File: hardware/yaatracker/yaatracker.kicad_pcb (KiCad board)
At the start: 2 copper layers, 63 parts, among them J1 USB_MINI, P1 TP_URX, P10 BATT, P11 MBUTTON2, P12 ICSP_CONN5, P13 I2C_SCREEN, P14 R_VCC, P15 GPS_DE9, P16 RADIO_DE9, P17 SW5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

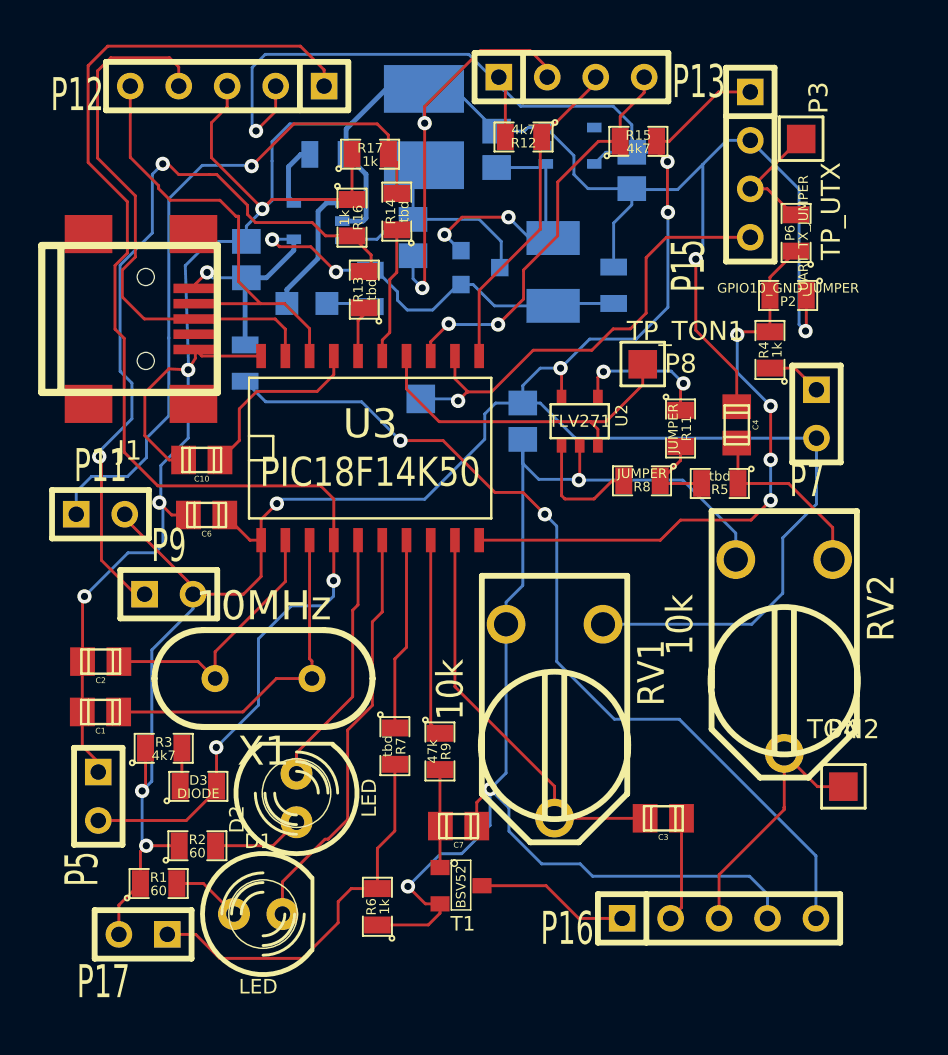
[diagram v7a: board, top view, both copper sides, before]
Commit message: PCB in the last stage
Layout done otherwise but need to see if can fix the "unconnected pad"
error - for some reason USB connector shield wants to be connected to a
data pin...
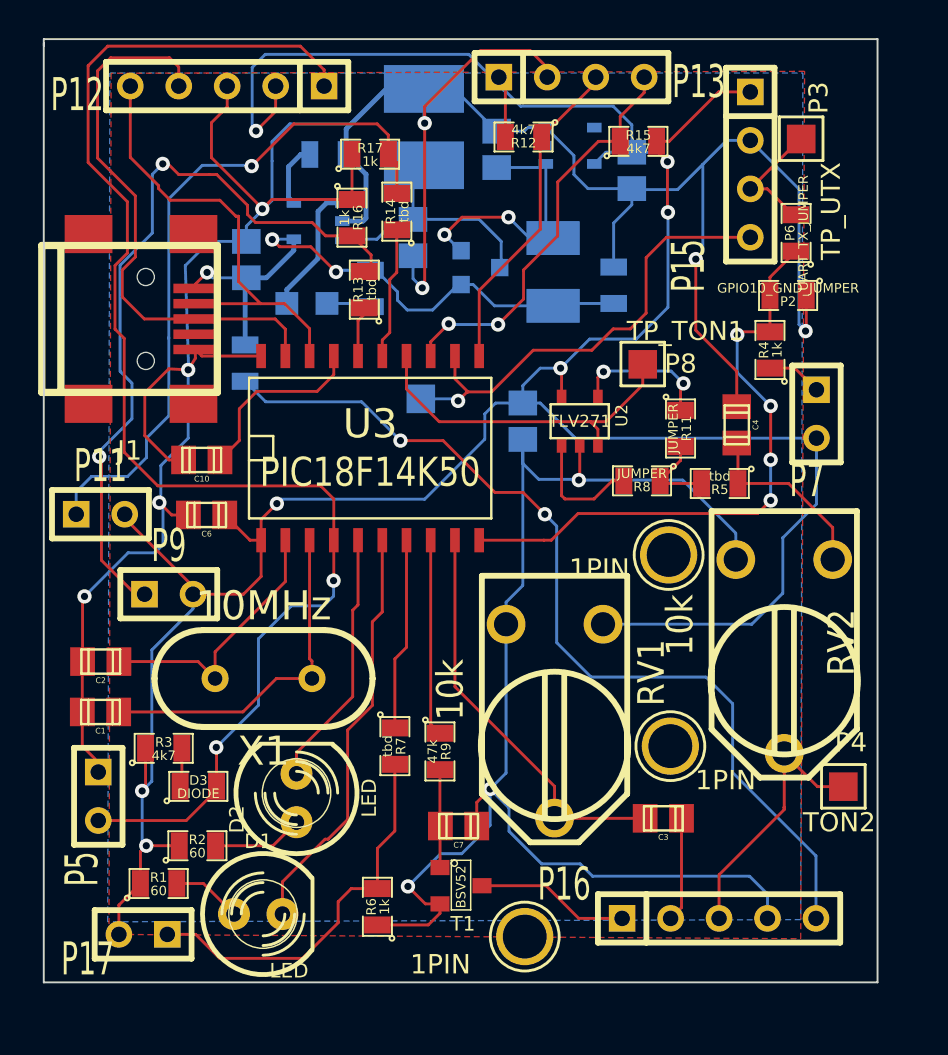
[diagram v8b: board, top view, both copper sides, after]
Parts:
- added 1PIN: P***, 1pin, F.Cu at (138.1, 145.0)
- added 1PIN: P***, 1pin, F.Cu at (138.2, 155.0)
- added 1PIN: P***, 1pin, F.Cu at (130.6, 165.0)
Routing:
- net /R_VOUT: track 47.7 -> 49.2 mm
- added copper zone on F.Cu, net +3.3V
- added copper zone on B.Cu, net GND
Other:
- board outline added: 43.7 x 49.4 mm
